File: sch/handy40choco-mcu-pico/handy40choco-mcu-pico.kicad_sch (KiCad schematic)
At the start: 15 parts, among them J1 Conn_01x02

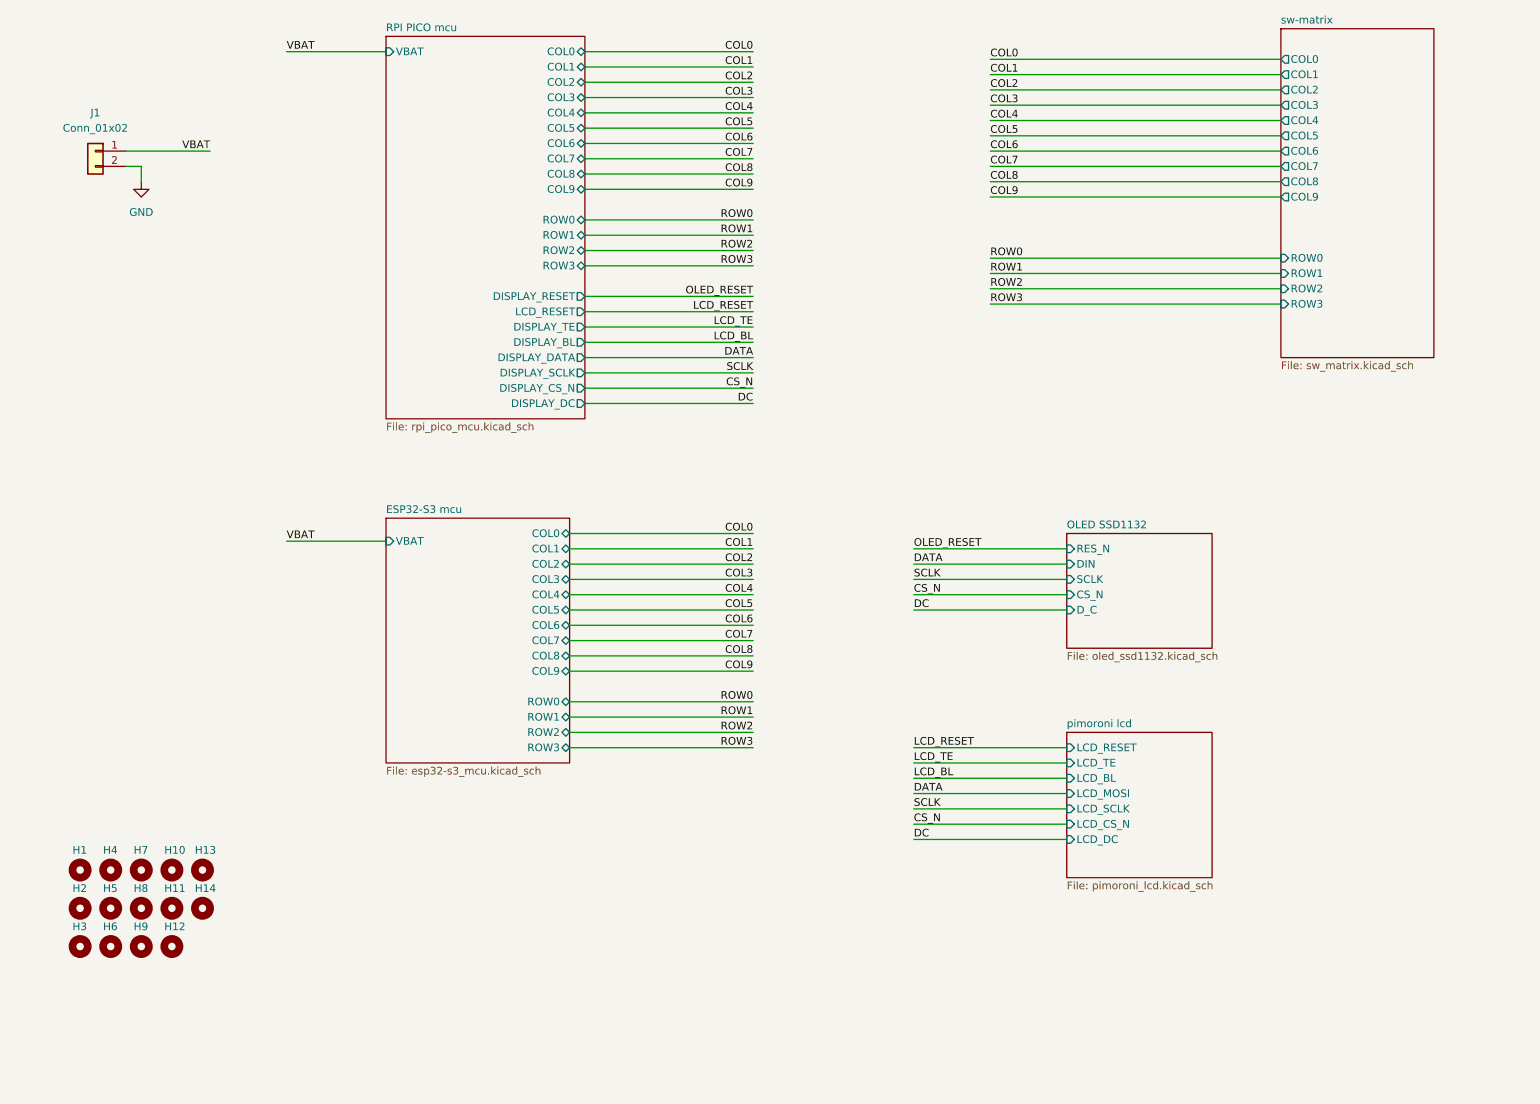
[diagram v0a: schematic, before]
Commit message: マイコン基板(pico)の雛形です。
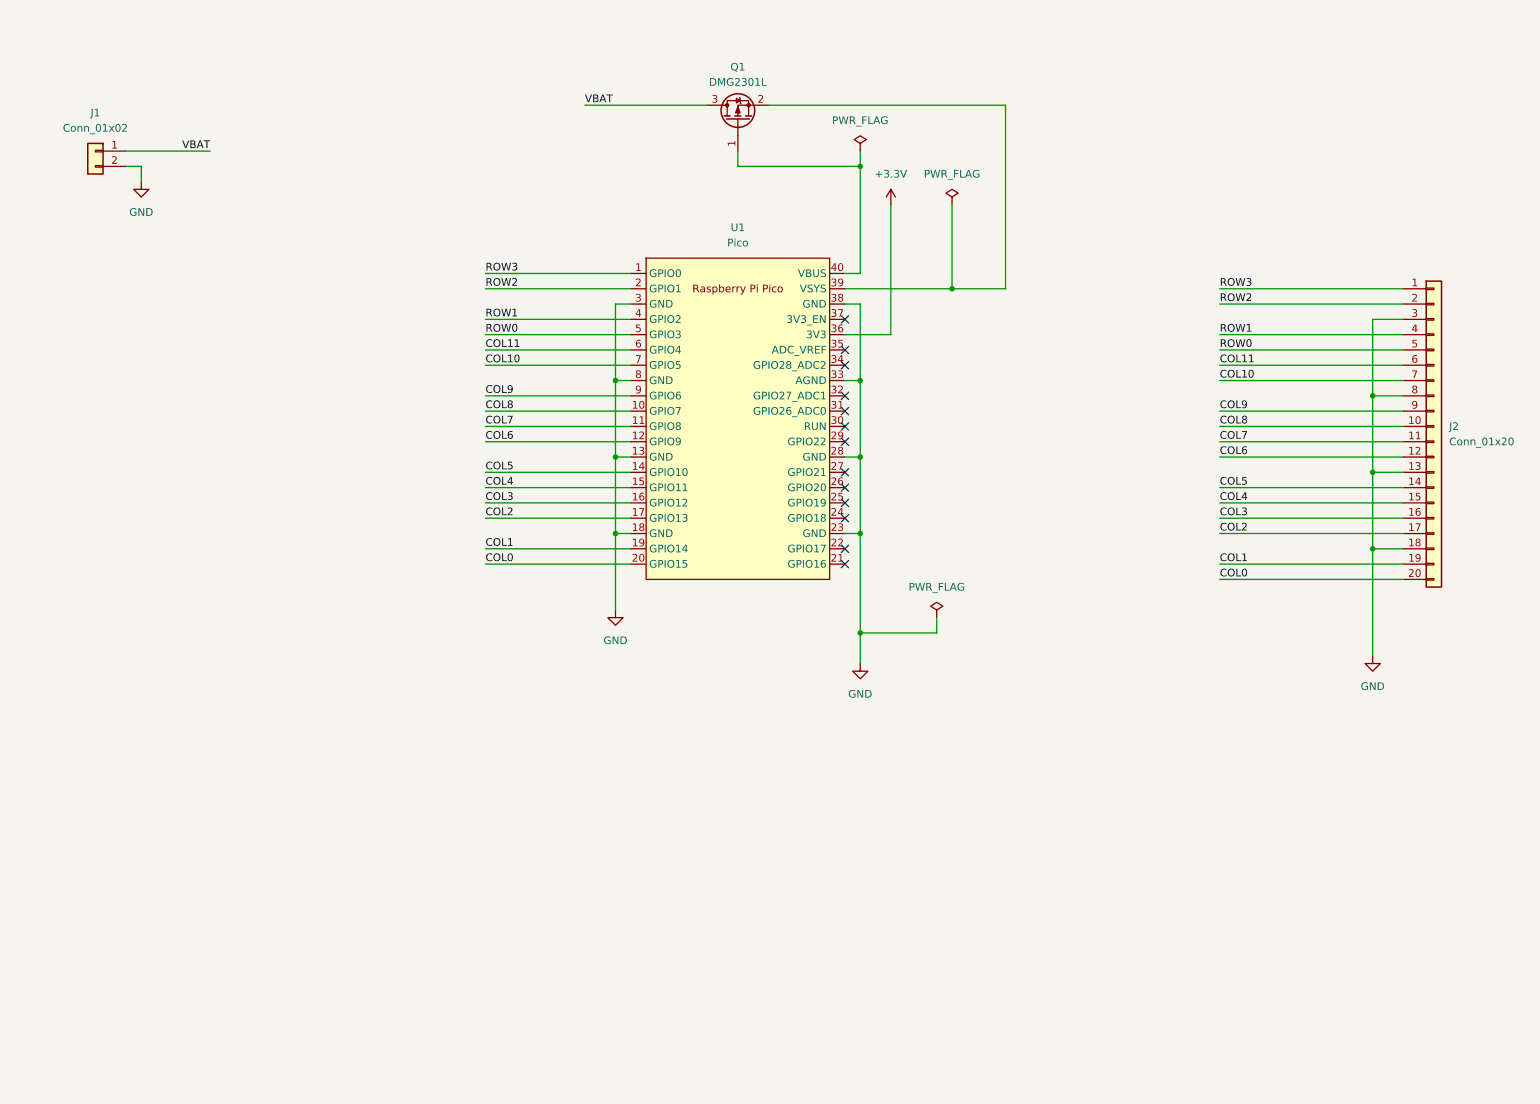
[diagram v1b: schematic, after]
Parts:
- removed H1, H10, H11, H12, H13, H14, H2, H3, H4, H5, H6, H7, H8, H9: MountingHole, my_keyswitch:my_MountingHole_2.2mm_M2, symbol Mechanical:MountingHole
- added J2: Conn_01x20, Connector_PinSocket_2.54mm:PinSocket_1x20_P2.54mm_Vertical, symbol Connector_Generic:Conn_01x20
- added Q1: DMG2301L, Package_TO_SOT_SMD:SOT-23, symbol Transistor_FET:DMG2301L
- added U1: Pico, my_pico:pico_no_dbg_smd_th_p0.85, symbol my_pico:my_pico_no_dbg
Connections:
- net COL0: now also J2.20 (Pin_20), U1.20 (GPIO15)
- net COL1: now also J2.19 (Pin_19), U1.19 (GPIO14)
- net COL2: now also J2.17 (Pin_17), U1.17 (GPIO13)
- net COL3: now also J2.16 (Pin_16), U1.16 (GPIO12)
- net COL4: now also J2.15 (Pin_15), U1.15 (GPIO11)
- net COL5: now also J2.14 (Pin_14), U1.14 (GPIO10)
- net COL6: now also J2.12 (Pin_12), U1.12 (GPIO9)
- net COL7: now also J2.11 (Pin_11), U1.11 (GPIO8)
- net COL8: now also J2.10 (Pin_10), U1.10 (GPIO7)
- net COL9: now also J2.9 (Pin_9), U1.9 (GPIO6)
- net GND: now also J2.13 (Pin_13), J2.18 (Pin_18), J2.3 (Pin_3), J2.8 (Pin_8), U1.13 (GND), U1.18 (GND), U1.23 (GND), U1.28 (GND), U1.3 (GND), U1.33 (AGND), U1.38 (GND), U1.8 (GND)
- net ROW0: now also J2.5 (Pin_5), U1.5 (GPIO3)
- net ROW1: now also J2.4 (Pin_4), U1.4 (GPIO2)
- net ROW2: now also J2.2 (Pin_2), U1.2 (GPIO1)
- net ROW3: now also J2.1 (Pin_1), U1.1 (GPIO0)
- net VBAT: now also Q1.3 (D)
- new net: Q1.1 (G), U1.40 (VBUS)
- new net: Q1.2 (S), U1.39 (VSYS)
- new net +3.3V: U1.36 (3V3)
- new net COL10: J2.7 (Pin_7), U1.7 (GPIO5)
- new net COL11: J2.6 (Pin_6), U1.6 (GPIO4)
- no-connect marks 0 -> 13
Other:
- removed sheet ESP32-S3 mcu
- removed sheet OLED SSD1132
- removed sheet RPI PICO mcu
- removed sheet pimoroni lcd
- removed sheet sw-matrix

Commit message: OLEDのコネクタを追加しました。
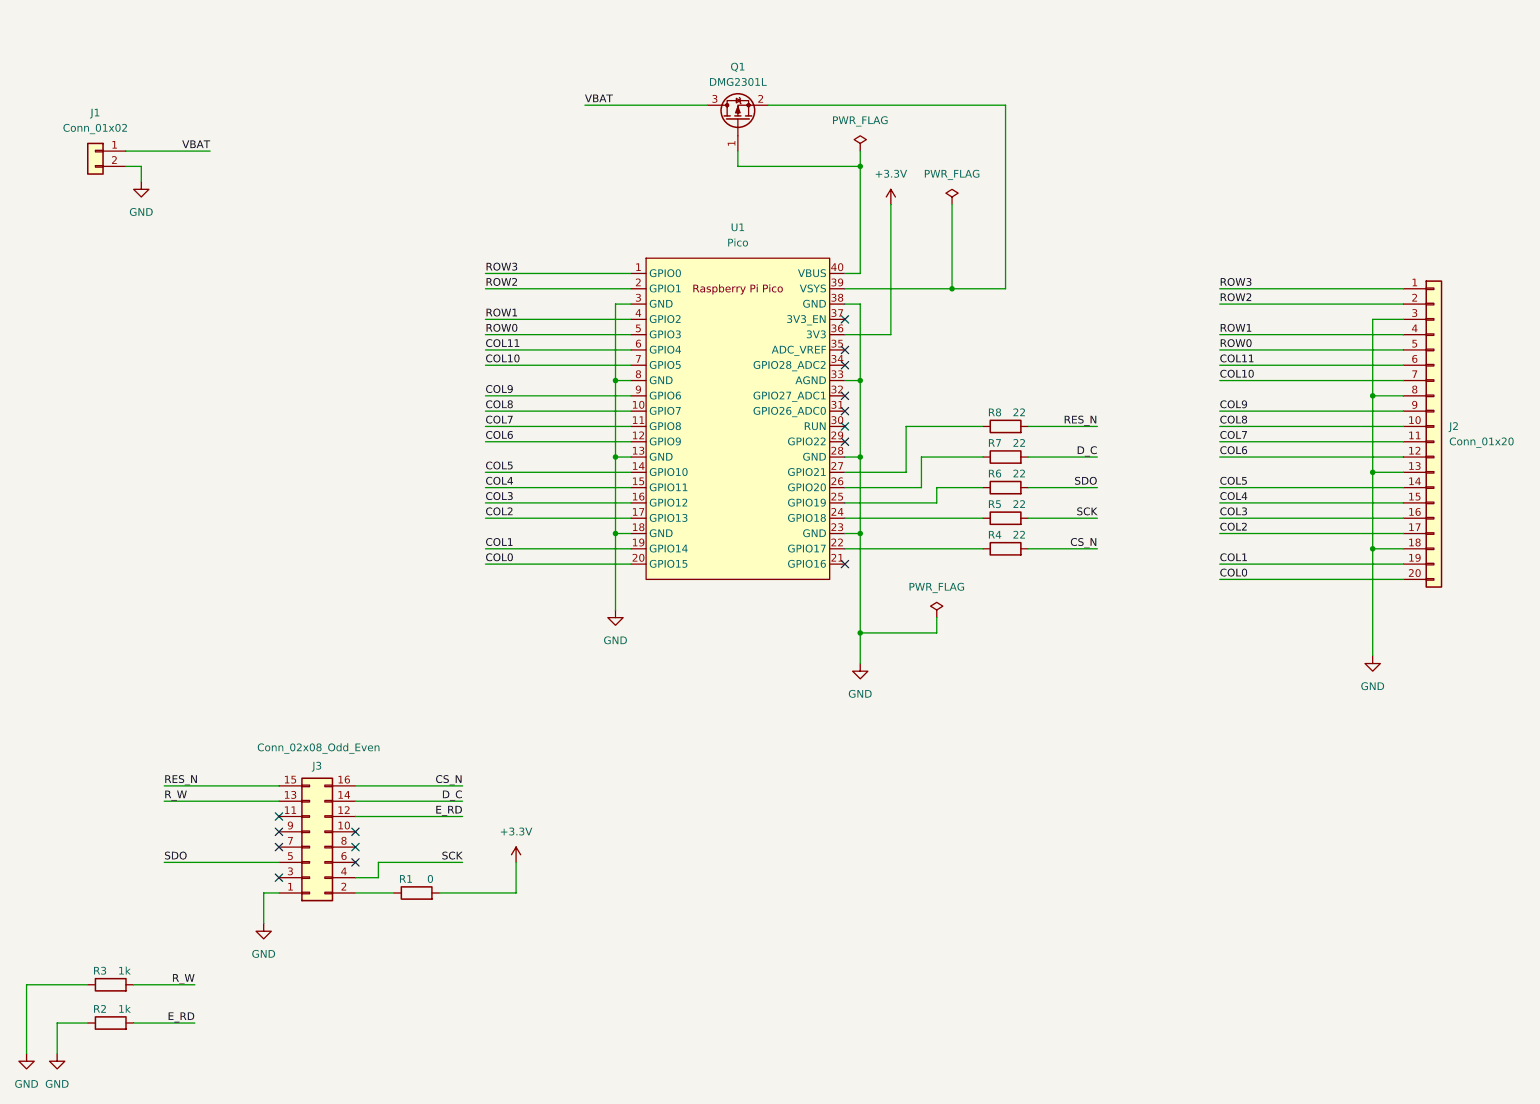
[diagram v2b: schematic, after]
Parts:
- added J3: Conn_02x08_Odd_Even, my_pico:oled_PinSocket_2x08_P2.54mm_Vertical, symbol Connector_Generic:Conn_02x08_Odd_Even
- added R1: 0, Resistor_SMD:R_0603_1608Metric_Pad0.98x0.95mm_HandSolder, symbol Device:R
- added R2, R3: 1k, Resistor_SMD:R_0603_1608Metric_Pad0.98x0.95mm_HandSolder, symbol Device:R
- added R4, R5, R6, R7, R8: 22, Resistor_SMD:R_0603_1608Metric_Pad0.98x0.95mm_HandSolder, symbol Device:R
- J2: footprint Connector_PinSocket_2.54mm:PinSocket_1x20_P2.54mm_Vertical -> my_keyswitch:my_PinHeader_1x20_P2.54mm_Vertical_p0.85
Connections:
- net +3.3V: now also R1.2
- net GND: now also J3.1 (Pin_1), R2.1, R3.1
- net at U1.22 (GPIO17): now also R4.1
- net at U1.24 (GPIO18): now also R5.1
- net at U1.25 (GPIO19): now also R6.1
- net at U1.26 (GPIO20): now also R7.1
- net at U1.27 (GPIO21): now also R8.1
- new net: J3.2 (Pin_2), R1.1
- new net CS_N: J3.16 (Pin_16), R4.2
- new net D_C: J3.14 (Pin_14), R7.2
- new net E_RD: J3.12 (Pin_12), R2.2
- new net RES_N: J3.15 (Pin_15), R8.2
- new net R_W: J3.13 (Pin_13), R3.2
- new net SCK: J3.4 (Pin_4), R5.2
- new net SDO: J3.5 (Pin_5), R6.2
- no-connect marks 13 -> 15

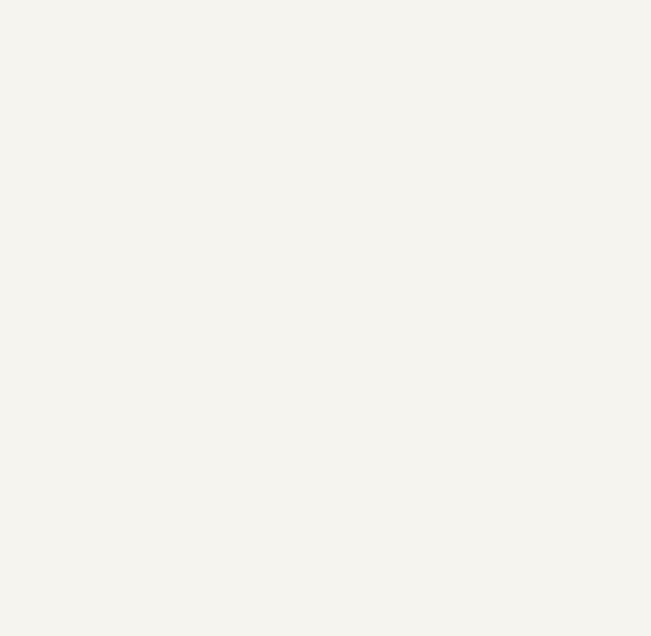
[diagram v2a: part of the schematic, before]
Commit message: ユニバーサル領域を追加しました。
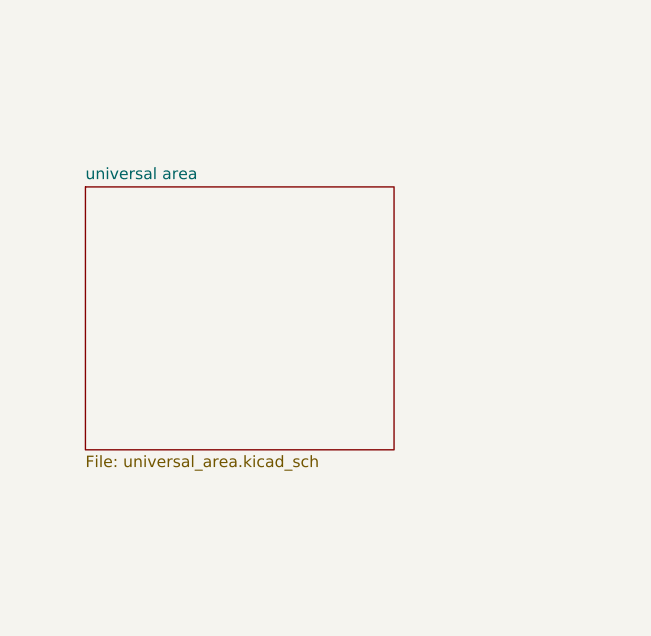
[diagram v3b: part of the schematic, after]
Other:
- added sheet universal area (universal_area.kicad_sch)
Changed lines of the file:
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@@
+		)
+	)
+	(sheet
+		(at 20.32 78.74)
+		(size 34.29 29.21)
+		(exclude_from_sim no)
+		(in_bom yes)
+		(on_board yes)
+		(dnp no)
+		(fields_autoplaced yes)
+		(stroke
+			(width 0.1524)
+			(type solid)
+		)
+		(fill
+			(color 0 0 0 0.0000)
+		)
+		(property "Sheetname" "universal area"
+			(at 20.32 78.0284 0)
+			(effects
+				(font
+					(size 1.27 1.27)
+				)
+				(justify left bottom)
+			)
+		)
+		(property "Sheetfile" "universal_area.kicad_sch"
+			(at 20.32 108.5346 0)
+			(effects
+				(font
+					(size 1.27 1.27)
+				)
+				(justify left top)
+			)
+		)
+		(instances
+			(project "handy40choco-mcu-pico"
+				(path "/c7705321-b11d-4074-930b-69ce3166659a"
+					(page "2")
+				)
+			)
 		)
 	)
